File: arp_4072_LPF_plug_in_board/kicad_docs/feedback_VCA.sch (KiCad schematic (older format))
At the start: 17 parts, among them Q10 MMBT3906, Q7 BCM847DS135, Q8 MMBT3904, Q9 MMBT3904, U2 TL072

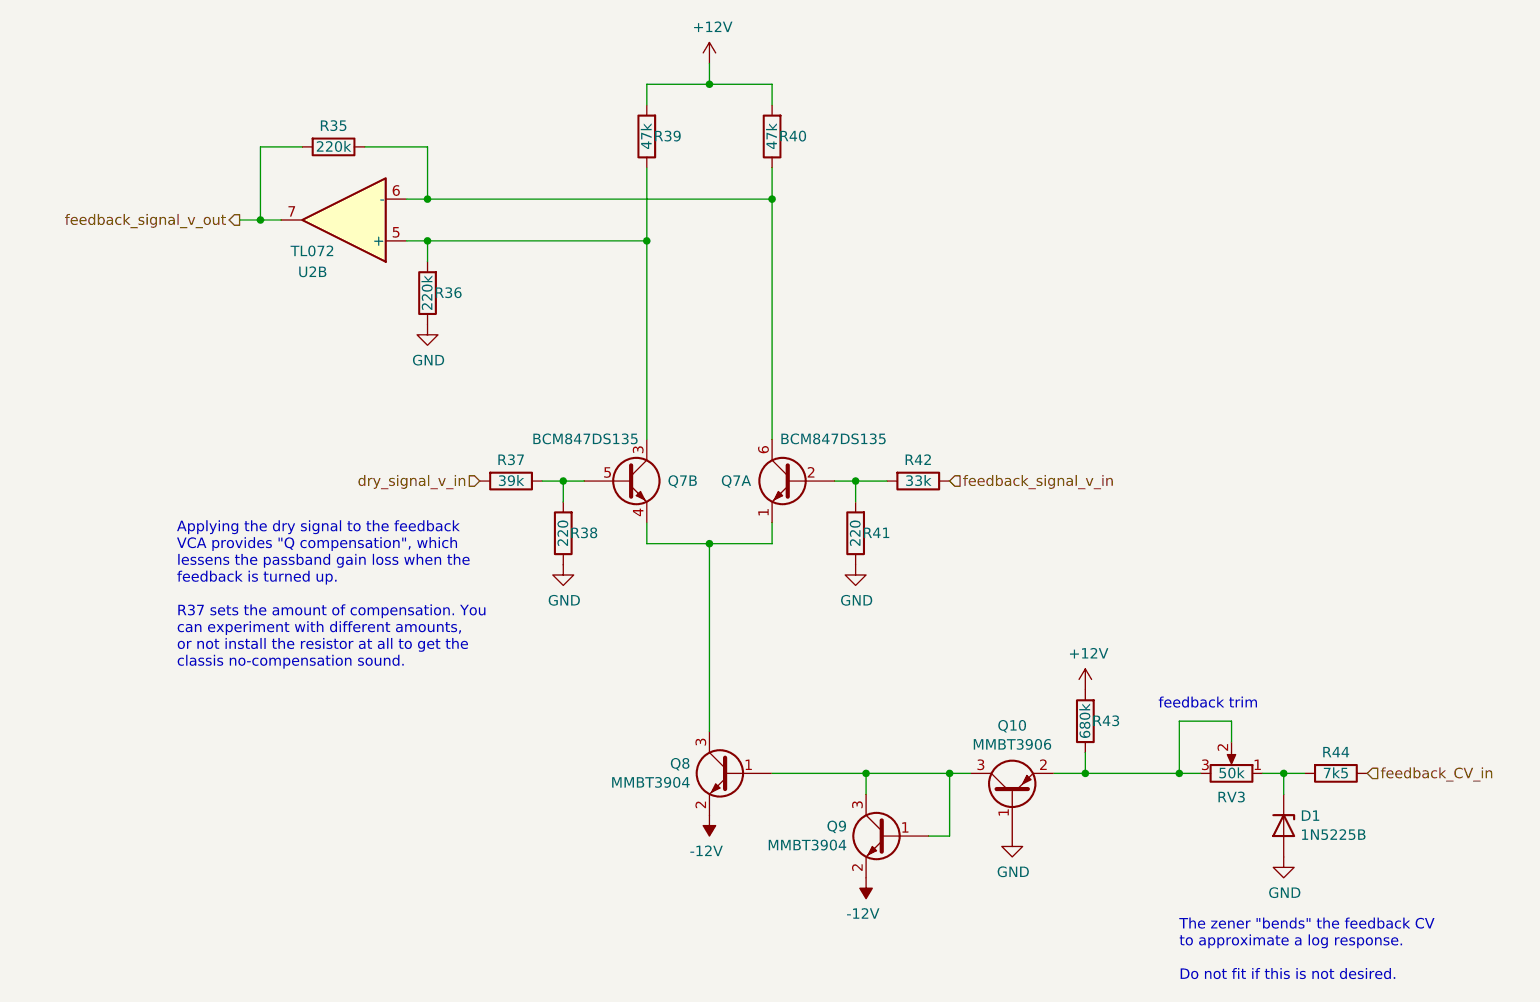
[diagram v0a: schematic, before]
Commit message: change zener value
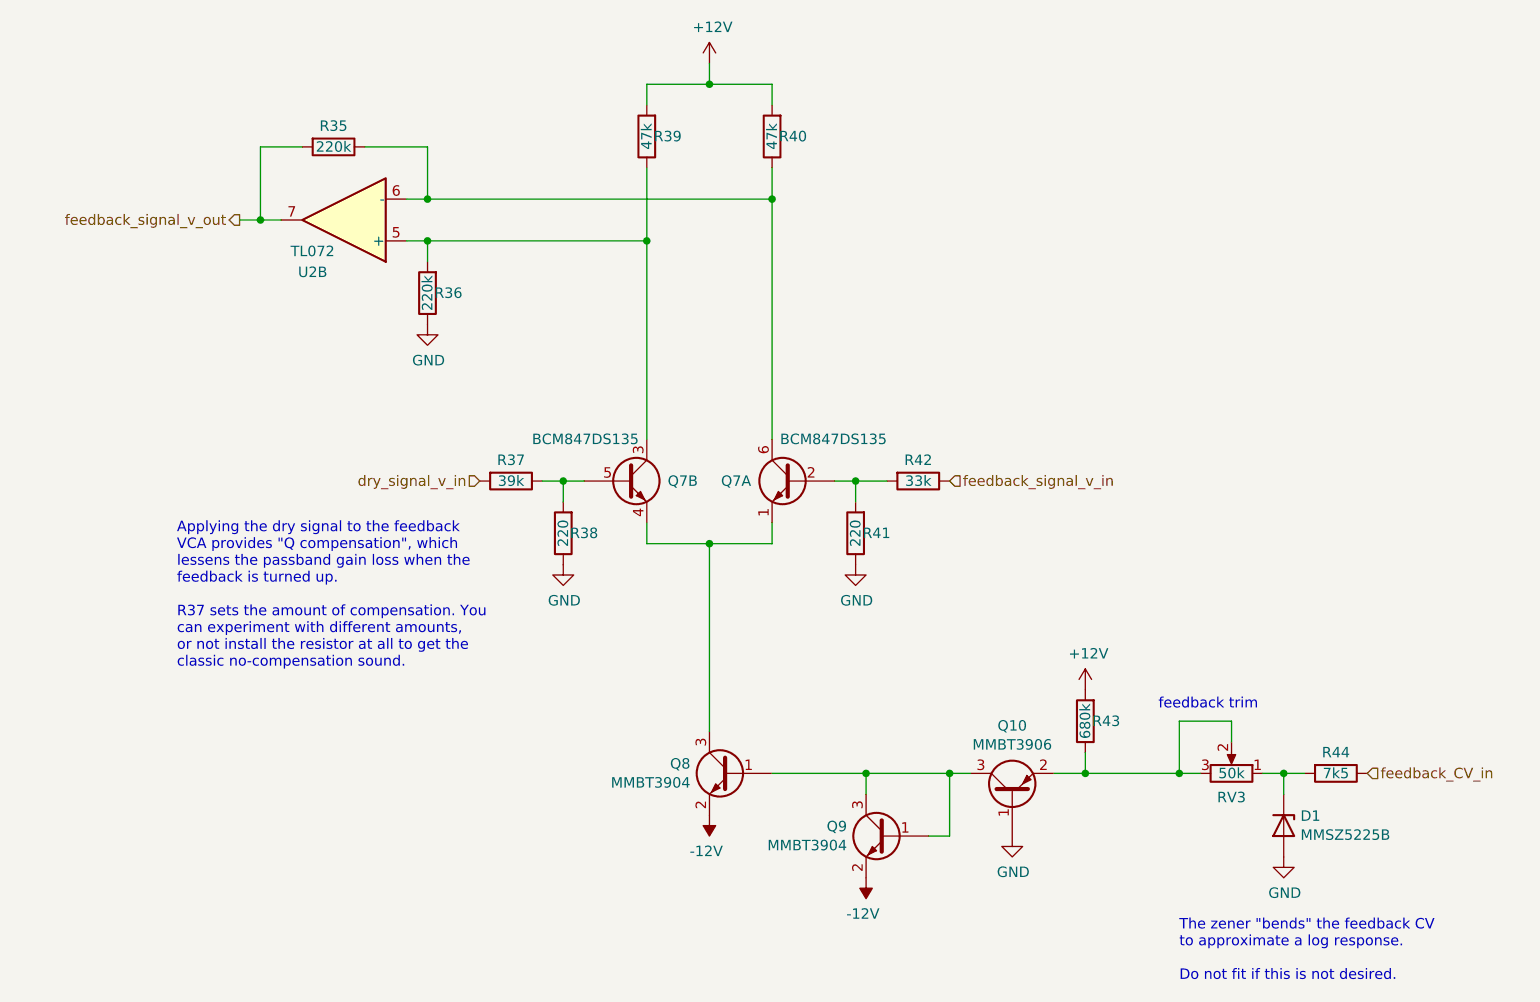
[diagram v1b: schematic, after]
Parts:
- D1: value 1N5225B -> MMSZ5225B
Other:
- note added: "Applying the dry signal to the feedback\nVCA provides "Q compensation", which\nlessens the passband gain loss when the\nfeedback is turned up.\n\nR37 sets the amount of compensation. You\ncan experiment with different amounts,\nor not install the resistor at all to get the \nclassic no-compensation sound.\n"
- note removed: "Applying the dry signal to the feedback\nVCA provides "Q compensation", which\nlessens the passband gain loss when the\nfeedback is turned up.\n\nR37 sets the amount of compensation. You\ncan experiment with different amounts,\nor not install the resistor at all to get the \nclassis no-compensation sound.\n"
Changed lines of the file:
@@
 P 8100 5200
 F 0 "D1" V 8054 5280 50  0000 L CNN
-F 1 "1N5225B" V 8145 5280 50  0000 L CNN
+F 1 "MMSZ5225B" V 8145 5280 50  0000 L CNN
 F 2 "Diode_SMD:D_SOD-123" H 8100 5200 50  0001 C CNN
 F 3 "~" H 8100 5200 50  0001 C CNN
@@
 Connection ~ 4650 3550
 Text Notes 2800 4450 0    50   ~ 0
-Applying the dry signal to the feedback\nVCA provides "Q compensation", which\nlessens the passband gain loss when the\nfeedback is turned up.\n\nR37 sets the amount of compensation. You\ncan experiment with different amounts,\nor not install the resistor at all to get the \nclassis no-compensation sound.\n
+Applying the dry signal to the feedback\nVCA provides "Q compensation", which\nlessens the passband gain loss when the\nfeedback is turned up.\n\nR37 sets the amount of compensation. You\ncan experiment with different amounts,\nor not install the resistor at all to get the \nclassic no-compensation sound.\n
 $EndSCHEMATC

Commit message: fix schemo and pcb problems
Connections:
- net at D1.1 (K), R44.2: now also RV3.3; no longer RV3.1
- net at Q10.2 (E), R43.1, RV3.2: now also RV3.1; no longer RV3.3
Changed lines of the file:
@@
 Sheet 5 5
 Title "ARP 4072 LPF"
-Date "2020-07-26"
-Rev "0"
+Date "2020-08-13"
+Rev "1"
 Comp ""
 Comment1 "creativecommons.org/licenses/by/4.0/"
@@
 P 3600 2300
 F 0 "U2" H 3750 2550 50  0000 C CNN
-F 1 "TL072" H 3750 2450 50  0000 C CNN
+F 1 "TL072" H 3750 2650 50  0000 C CNN
 F 2 "Package_SO:SOIC-8_3.9x4.9mm_P1.27mm" H 3600 2300 50  0001 C CNN
 F 3 "http://www.ti.com/lit/ds/symlink/tl071.pdf" H 3600 2300 50  0001 C CNN
@@
 U 1 1 5F0E044B
 P 4000 2650
-F 0 "R36" H 3900 2650 50  0000 C CNN
+F 0 "R36" H 3850 2650 50  0000 C CNN
 F 1 "220k" V 4000 2650 50  0000 C CNN
 F 2 "Resistor_SMD:R_0805_2012Metric_Pad1.15x1.40mm_HandSolder" V 3930 2650 50  0001 C CNN
@@
 U 1 1 5F0ECB62
 P 5050 1900
-F 0 "R39" H 4950 1900 50  0000 C CNN
+F 0 "R39" H 4900 1900 50  0000 C CNN
 F 1 "47k" V 5050 1900 50  0000 C CNN
 F 2 "Resistor_SMD:R_0805_2012Metric_Pad1.15x1.40mm_HandSolder" V 4980 1900 50  0001 C CNN
@@
 U 1 1 5F0ED8A9
 P 5650 1900
-F 0 "R40" H 5550 1900 50  0000 C CNN
+F 0 "R40" H 5500 1900 50  0000 C CNN
 F 1 "47k" V 5650 1900 50  0000 C CNN
 F 2 "Resistor_SMD:R_0805_2012Metric_Pad1.15x1.40mm_HandSolder" V 5580 1900 50  0001 C CNN
@@
 U 1 1 5F0EDC2E
 P 4650 3800
-F 0 "R38" H 4550 3800 50  0000 C CNN
+F 0 "R38" H 4500 3800 50  0000 C CNN
 F 1 "220" V 4650 3800 50  0000 C CNN
 F 2 "Resistor_SMD:R_0805_2012Metric_Pad1.15x1.40mm_HandSolder" V 4580 3800 50  0001 C CNN
@@
 U 1 1 5F0EEFAD
 P 6050 3800
-F 0 "R41" H 5950 3800 50  0000 C CNN
+F 0 "R41" H 5900 3800 50  0000 C CNN
 F 1 "220" V 6050 3800 50  0000 C CNN
 F 2 "Resistor_SMD:R_0805_2012Metric_Pad1.15x1.40mm_HandSolder" V 5980 3800 50  0001 C CNN
@@
 F 3 "~" H 7850 4950 50  0001 C CNN
 	1    7850 4950
-	0    1    -1   0
+	0    -1   -1   0
 $EndComp
 Wire Wire Line
@@
 U 1 1 5F100ACF
 P 7150 4700
-F 0 "R43" H 7050 4700 50  0000 C CNN
+F 0 "R43" H 7000 4700 50  0000 C CNN
 F 1 "680k" V 7150 4700 50  0000 C CNN
 F 2 "Resistor_SMD:R_0805_2012Metric_Pad1.15x1.40mm_HandSolder" V 7080 4700 50  0001 C CNN
